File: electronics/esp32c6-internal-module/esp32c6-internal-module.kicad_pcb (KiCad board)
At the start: 2 copper layers, 17 x 38 mm, 30 parts, among them J1 USB_C_SOCKET_RA_PTH_SIMPLE, P1 JST_SH_4_RA, P2 CONN_01X06, SW1 B3U-1000P_SPST-NO_SMD, SW2 B3U-1000P_SPST-NO_SMD, U1 ESP32-C6-MINI-1, U2 TLV76733DRV, U3 USBLC6

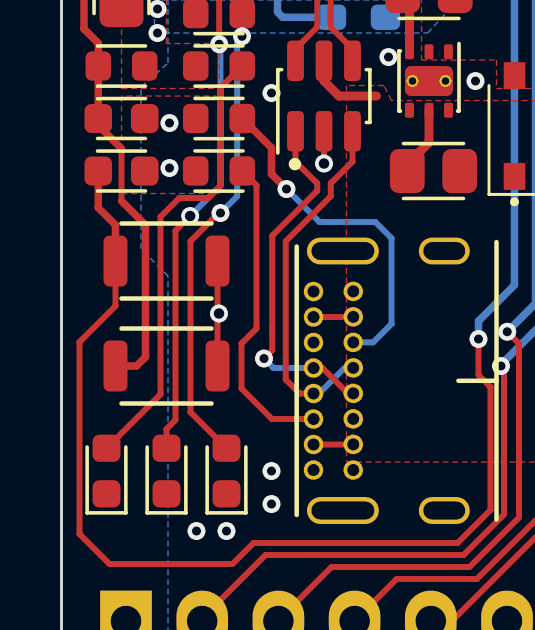
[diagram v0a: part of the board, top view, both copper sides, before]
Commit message: Add manufacturing exports for C6 internal module board
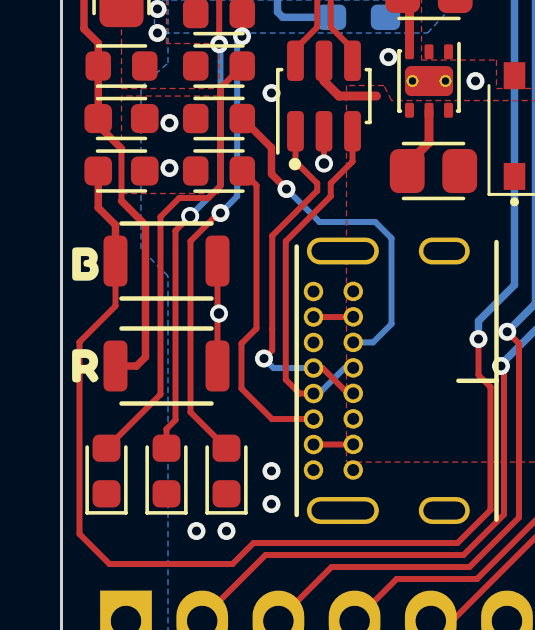
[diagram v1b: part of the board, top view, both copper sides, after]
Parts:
- added kibuzzard-6671475C: G***, kibuzzard-6671475C, B.Cu at (102.2, 93.5)
- added kibuzzard-66714795: G***, kibuzzard-66714795, B.Cu at (114.8, 93.6)
- added kibuzzard-66714802: G***, kibuzzard-66714802, B.Cu at (111.0, 93.6)
- added kibuzzard-6671480C: G***, kibuzzard-6671480C, B.Cu at (112.7, 93.6)
- added kibuzzard-6671482E: G***, kibuzzard-6671482E, B.Cu at (107.0, 93.5)
- added kibuzzard-66714835: G***, kibuzzard-66714835, B.Cu at (104.7, 93.5)
- added kibuzzard-66714898: G***, kibuzzard-66714898, B.Cu at (101.2, 79.1)
- added kibuzzard-667148AD: G***, kibuzzard-667148AD, B.Cu at (106.7, 77.2)
- added kibuzzard-667148E1: G***, kibuzzard-667148E1, B.Cu at (101.2, 70.8)
- added kibuzzard-66714909: G***, kibuzzard-66714909, F.Cu at (100.8, 89.5)
- added kibuzzard-66714928: G***, kibuzzard-66714928, F.Cu at (100.8, 86.1)
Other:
- board text added: "2-layer 1.6mm FR4 38x17 mm outline 35 um (1oz) copper weight HASL finish acceptable 0.2 mm minimum trace/clearance 0.3 mm minimum via drill"
- board text added: "PCB ORDER NOTES"
